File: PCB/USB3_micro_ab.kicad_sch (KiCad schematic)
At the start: 9 parts, among them IC1108 IP4220CZ6, J2 USB3_B_Micro

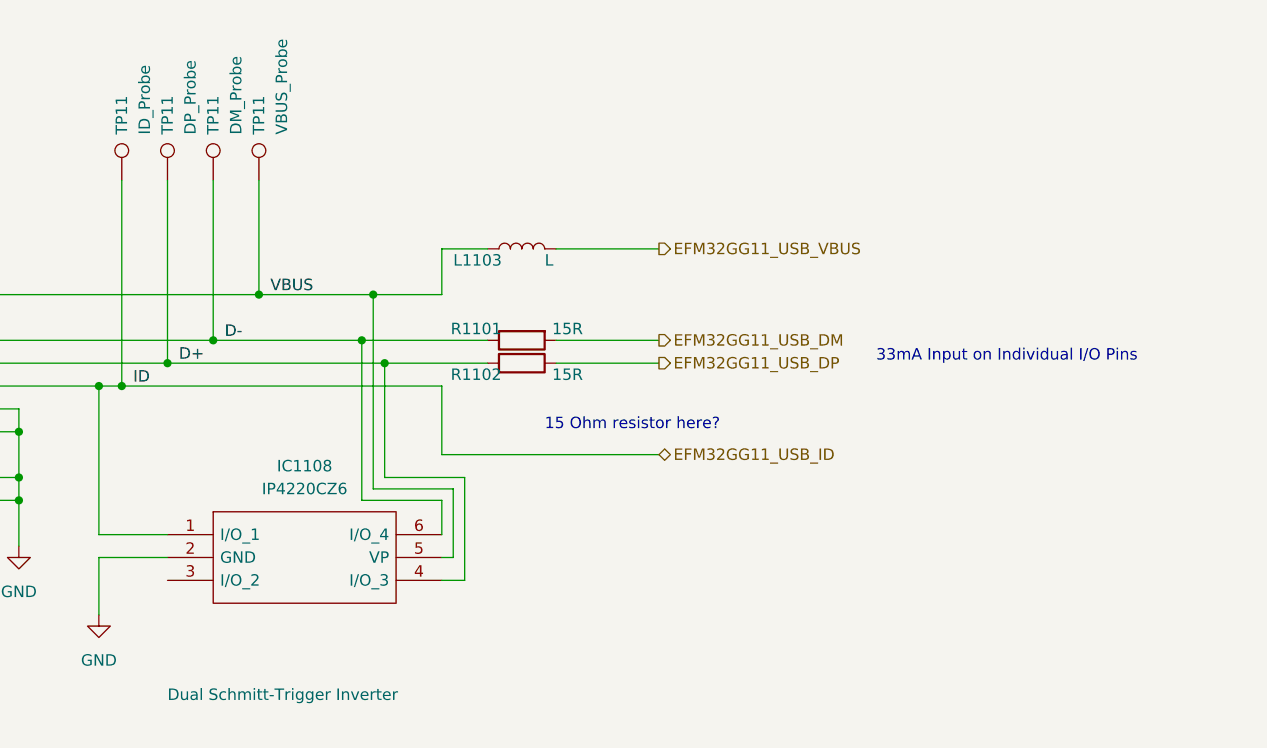
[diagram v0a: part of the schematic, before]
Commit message: Attempt to set up SRAM
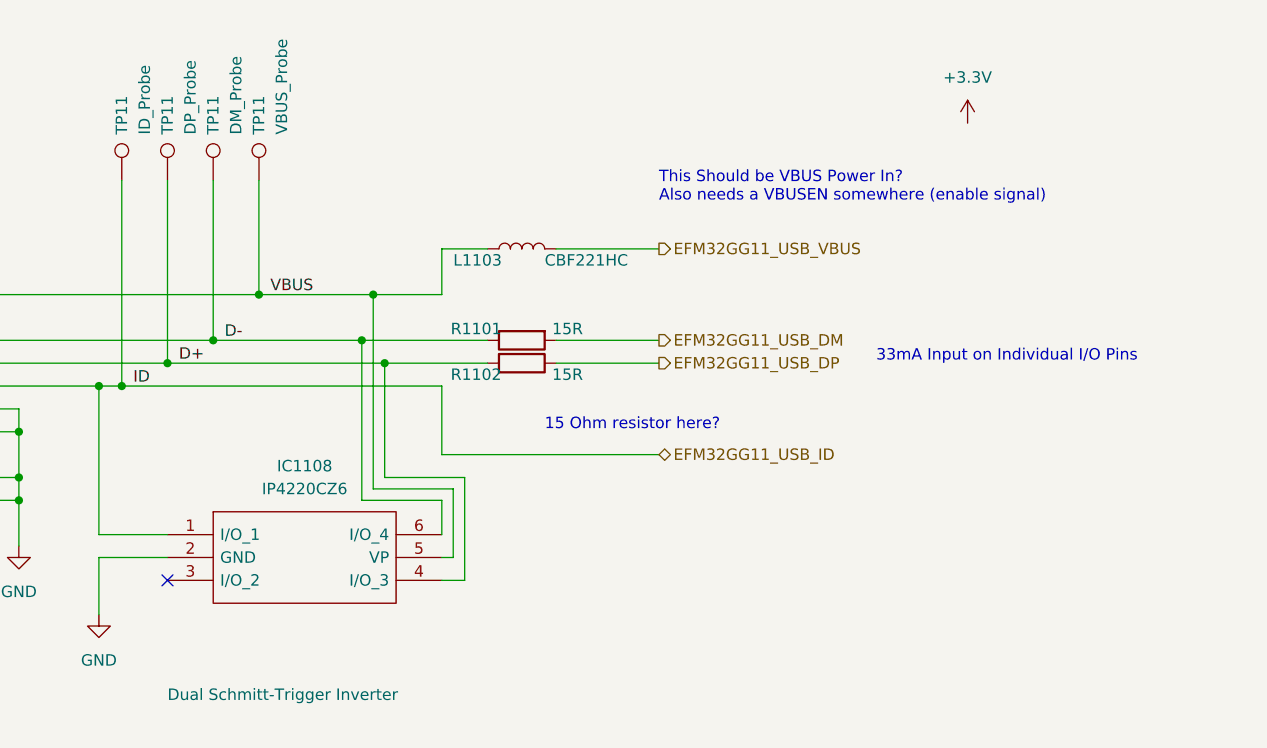
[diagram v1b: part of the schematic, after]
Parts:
- L1103: value L -> CBF221HC
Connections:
- no-connect marks 0 -> 1
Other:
- note added: "This Should be VBUS Power In? Also needs a VBUSEN somewhere (enable signal)"
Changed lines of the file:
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@@
   (junction (at 113.03 92.71) (diameter 0) (color 0 0 0 0)
   )
+  (no_connect (at 118.11 114.3))
   (wire (pts (xy 113.03 92.71) (xy 148.59 92.71))
     (stroke (width 0) (type default))
@@
   )
   (text "15 Ohm resistor here?\n" (at 160.02 97.79 0)
+    (effects (font (size 1.27 1.27)) (justify left bottom))
+  )
+  (text "This Should be VBUS Power In?\nAlso needs a VBUSEN somewhere (enable signal)\n"
+    (at 172.72 72.39 0)
     (effects (font (size 1.27 1.27)) (justify left bottom))
   )
@@
         (path "/e9047d94-28be-4266-894b-6ee25ef088bd/f9a74965-bde5-47a2-9f66-243cb6fc0f53/f8dfcd07-d713-410a-88b5-31ae3a6c85dd"
           (reference "R1101") (unit 1)
+        )
+      )
+    )
+  )
+  (symbol (lib_id "power:+3.3V") (at 207.01 63.5 0) (unit 1)
+    (in_bom yes) (on_board yes) (dnp no) (fields_autoplaced)
+    (property "Reference" "#PWR017" (at 207.01 67.31 0)
+      (effects (font (size 1.27 1.27)) hide)
+    )
+    (property "Value" "+3.3V" (at 207.01 58.42 0)
+      (effects (font (size 1.27 1.27)))
+    )
+    (property "Footprint" "" (at 207.01 63.5 0)
+      (effects (font (size 1.27 1.27)) hide)
+    )
+    (property "Datasheet" "" (at 207.01 63.5 0)
+      (effects (font (size 1.27 1.27)) hide)
+    )
+    (pin "1")
+    (instances
+      (project "RayTracingPCB"
+        (path "/e9047d94-28be-4266-894b-6ee25ef088bd/f9a74965-bde5-47a2-9f66-243cb6fc0f53"
+          (reference "#PWR017") (unit 1)
+        )
+        (path "/e9047d94-28be-4266-894b-6ee25ef088bd/f9a74965-bde5-47a2-9f66-243cb6fc0f53/f8dfcd07-d713-410a-88b5-31ae3a6c85dd"
+          (reference "#PWR021") (unit 1)
         )
       )
@@
       (effects (font (size 1.27 1.27)) (justify left))
     )
-    (property "Value" "L" (at 160.02 78.74 90)
+    (property "Value" "CBF221HC" (at 160.02 78.74 90)
       (effects (font (size 1.27 1.27)) (justify left))
     )

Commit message: dump
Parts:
- added C31: 10nF, symbol Device:C_Small
- added C32: 100nF, symbol Device:C_Small
- added C33: 4.7uF, symbol Device:C_Small
- added FB1: FerriteBead, symbol Device:FerriteBead_Small
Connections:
- net GND: now also C31.2, C32.2, C33.2
- net VBUS: now also C31.1, FB1.1
- new net +5V: C32.1, C33.1, FB1.2

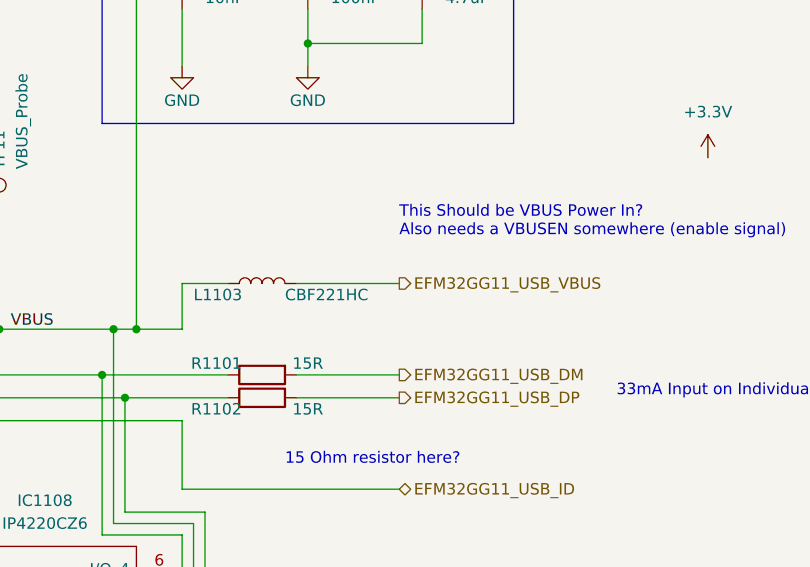
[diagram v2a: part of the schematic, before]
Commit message: Clean up MCU ++
Signed-off-by: Daniel Yang Hansen <daniel.yang.hansen@gmail.com>
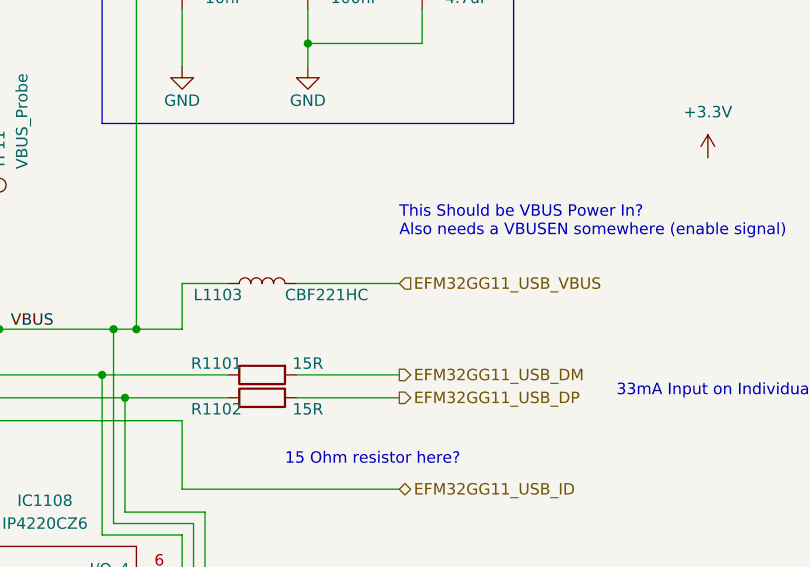
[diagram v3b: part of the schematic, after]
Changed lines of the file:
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@@
     (effects (font (size 1.27 1.27)) (justify left))
   )
-  (hierarchical_label "EFM32GG11_USB_VBUS" (shape output) (at 172.72 77.47 0) (fields_autoplaced)
+  (hierarchical_label "EFM32GG11_USB_VBUS" (shape input) (at 172.72 77.47 0) (fields_autoplaced)
     (effects (font (size 1.27 1.27)) (justify left))
   )
